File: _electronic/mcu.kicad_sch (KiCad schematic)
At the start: 3 parts

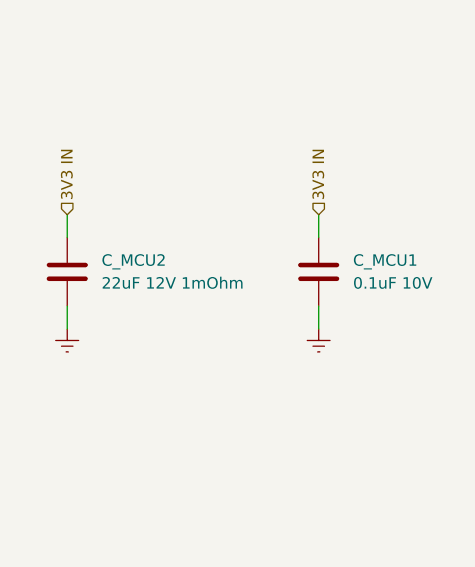
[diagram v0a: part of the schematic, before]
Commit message: organized electronics folder
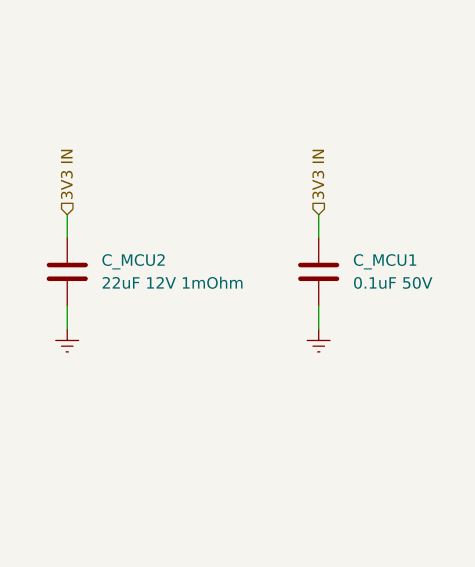
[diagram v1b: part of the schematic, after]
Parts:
- C_MCU1: value 0.1uF 10V -> 0.1uF 50V; # CGA3E2X7R1H104K080AA -> C1608X7R1H104K080AA
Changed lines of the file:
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@@
       (effects (font (size 1.27 1.27)) (justify left))
     )
-    (property "Value" "0.1uF 10V" (id 1) (at 228.6 107.95 0)
+    (property "Value" "0.1uF 50V" (id 1) (at 228.6 107.95 0)
       (effects (font (size 1.27 1.27)) (justify left))
     )
@@
       (effects (font (size 1.27 1.27)) hide)
     )
-    (property "#" "CGA3E2X7R1H104K080AA" (id 4) (at 228.6 106.68 0)
+    (property "#" "C1608X7R1H104K080AA" (id 4) (at 228.6 106.68 0)
       (effects (font (size 1.27 1.27) italic) (justify left) hide)
     )

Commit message: v1 pcb
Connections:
- net IO26 BUZZER OUT: now reaches U_MCU1.11 (IO26)
- net IO27 BUZZER OUT: no longer names the net of U_MCU1.12 (IO27)
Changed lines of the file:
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@@
   (no_connect (at 123.19 115.57))
   (no_connect (at 158.75 90.17))
+  (no_connect (at 158.75 123.19))
   (no_connect (at 158.75 133.35))
   (no_connect (at 123.19 110.49))
-  (no_connect (at 158.75 120.65))
   (no_connect (at 123.19 82.55))
   (no_connect (at 158.75 107.95))
@@
     (stroke (width 0) (type default) (color 0 0 0 0))
   )
+  (wire (pts (xy 158.75 123.19) (xy 156.21 123.19))
+    (stroke (width 0) (type default) (color 0 0 0 0))
+  )
   (wire (pts (xy 160.02 130.81) (xy 156.21 130.81))
     (stroke (width 0) (type default) (color 0 0 0 0))
@@
     (stroke (width 0) (type default) (color 0 0 0 0))
   )
-  (wire (pts (xy 156.21 123.19) (xy 160.02 123.19))
+  (wire (pts (xy 156.21 120.65) (xy 160.02 120.65))
     (stroke (width 0) (type default) (color 0 0 0 0))
   )
@@
   )
   (wire (pts (xy 123.19 118.11) (xy 125.73 118.11))
-    (stroke (width 0) (type default) (color 0 0 0 0))
-  )
-  (wire (pts (xy 158.75 120.65) (xy 156.21 120.65))
     (stroke (width 0) (type default) (color 0 0 0 0))
   )
@@
     (effects (font (size 1.27 1.27)) (justify left))
   )
-  (hierarchical_label "IO27 BUZZER OUT" (shape input) (at 160.02 123.19 0)
+  (hierarchical_label "IO26 BUZZER OUT" (shape input) (at 160.02 120.65 0)
     (effects (font (size 1.27 1.27)) (justify left))
   )

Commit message: led resistor revision, b.o.m. and pcb anotation
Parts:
- C_MCU2: value 22uF 12V 1mOhm -> 10uF 12V; # CL10A226MO7JZNC -> GRM188Z71A106KA73D
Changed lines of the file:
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@@
       (effects (font (size 1.27 1.27)) (justify right))
     )
-    (property "Value" "22uF 12V 1mOhm" (id 1) (at 200.66 107.95 0)
+    (property "Value" "10uF 12V" (id 1) (at 200.66 107.95 0)
       (effects (font (size 1.27 1.27)) (justify right))
     )
@@
       (effects (font (size 1.27 1.27)) hide)
     )
-    (property "#" "CL10A226MO7JZNC" (id 4) (at 200.66 106.68 0)
+    (property "#" "GRM188Z71A106KA73D" (id 4) (at 200.66 106.68 0)
       (effects (font (size 1.27 1.27) italic) (justify right) hide)
     )

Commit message: schematics and pcb cleanup
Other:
- title: E-TKT -> E-TKT v1.0
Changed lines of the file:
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@@
   (paper "A4")
   (title_block
-    (title "E-TKT")
-    (date "2022-07-21")
-    (rev "3")
+    (title "E-TKT v1.0")
+    (date "2022-09-29")
+    (rev "4")
     (company "Andrei Speridiao")
   )
